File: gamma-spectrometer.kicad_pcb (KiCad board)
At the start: 2 copper layers, 140.3 x 36.5 mm, 71 parts, among them J1 *, J2 *, Q1 2N7002, Q3 MMBT5088LT1G, Q4 MMBT5088LT1G, U1 Pico 2, U10 MICROFC-60035-SMT-TR1, U2 OPA357AIDBVR, U3 TLV3201AIDBVR, U4 OPA357AIDBVR, U5 OPA357AIDBVR, U6 LM4040AIM3-3.0+T, U7 LM4040AIM3-3.0+T, U8 MAX5026EUT_T, U9 TPS7B6950DBVR

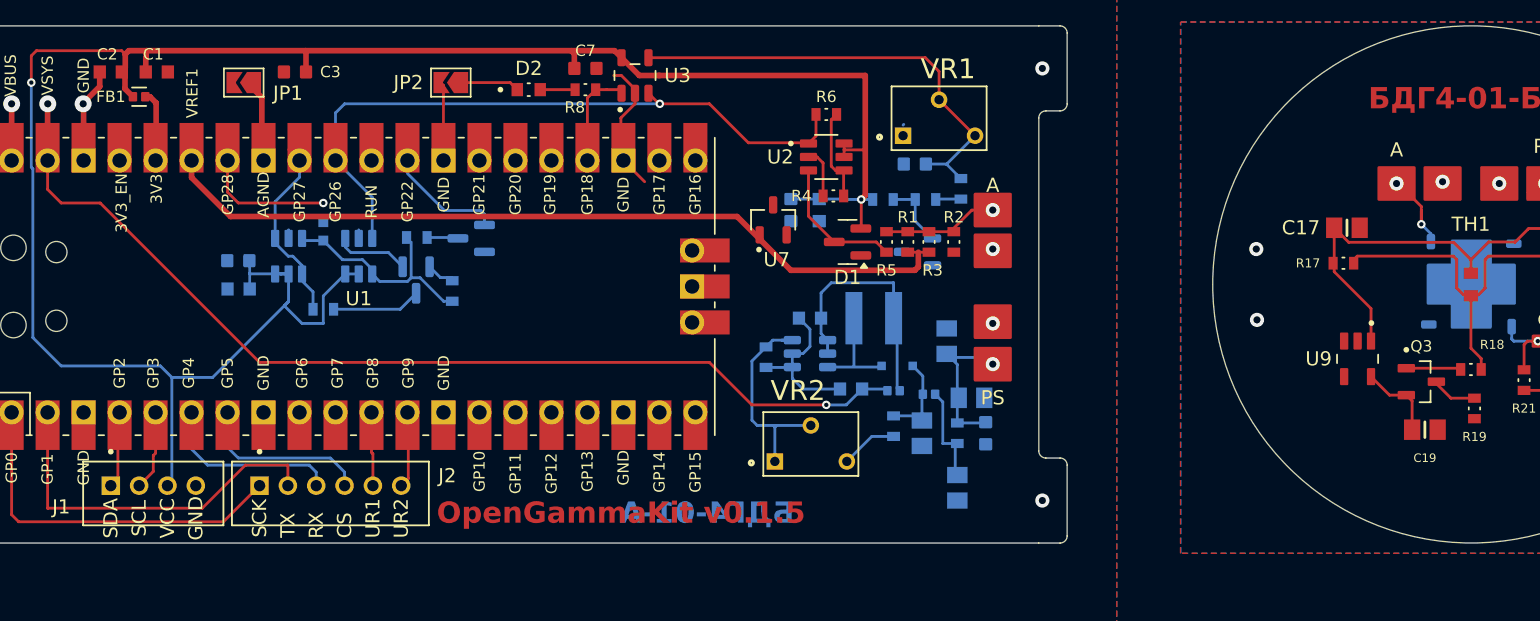
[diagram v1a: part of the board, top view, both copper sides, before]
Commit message: C17,C19,FB1,FB2,FB3 footprint fix
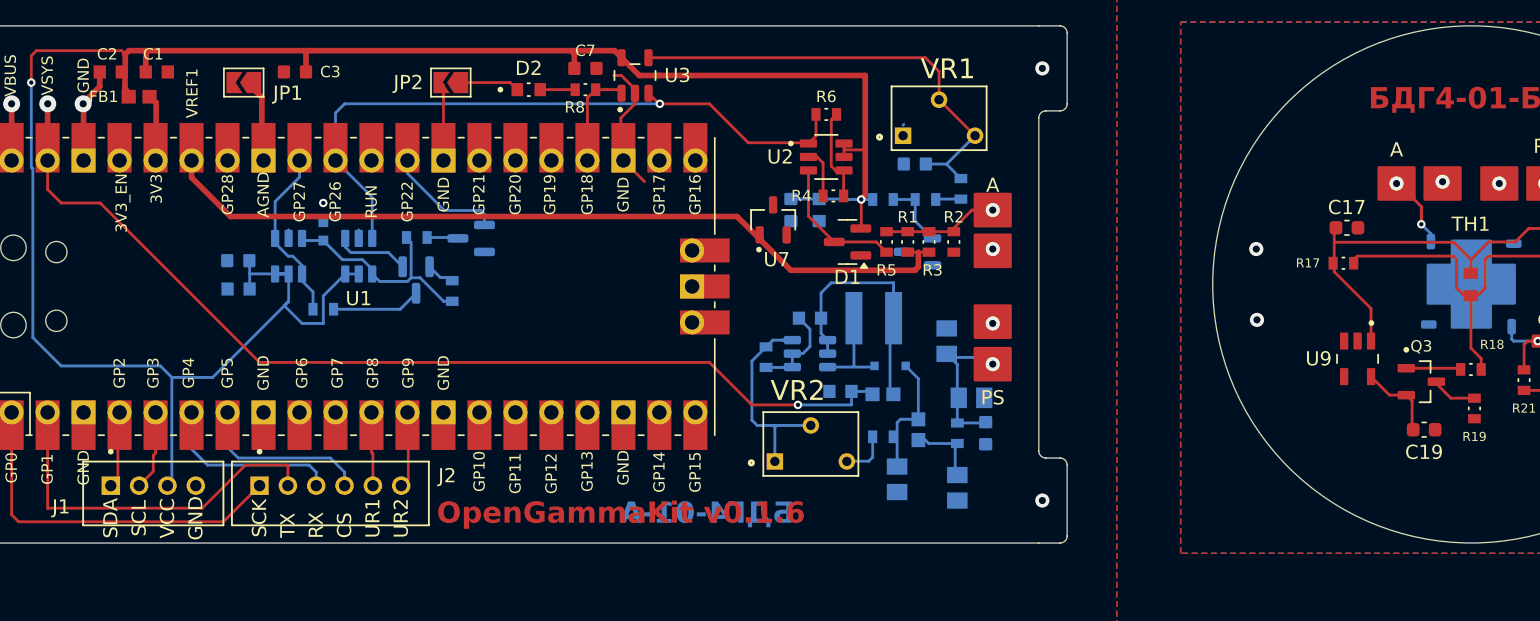
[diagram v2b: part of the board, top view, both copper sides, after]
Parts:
- C17, C19: footprint CL21A475KBQNNNE:CAPC2012X140N -> Capacitor_SMD:C_0603_1608Metric
- FB1, FB2, FB3: footprint ACML-0402HC-301-T:BEADC1005X65N -> BLM18KG102SN1D:BEADC1608X95N
- moved C12 3.69 mm to (152.0, 97.5)
- moved FB2 2.61 mm to (153.5, 94.0), turned to 90 degrees
- moved R15 1.06 mm to (151.0, 94.5), turned to 0 degrees
- moved FB3 0.79 mm to (151.0, 91.5)
- moved C18 0.77 mm to (148.0, 91.3)
- moved D5 0.50 mm to (151.5, 89.5)
- moved C19 0.05 mm to (189.2, 94.0)
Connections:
- net Net-(U8-VCC) renamed Vdrive
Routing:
- net GND: track 50.1 -> 36.4 mm
- net Net-(D5-K): track 6.31 -> 8.84 mm
- net Net-(C13-Pad1): track 7.06 -> 5.19 mm
- net Vdrive: track 18.0 -> 18.6 mm
- net Net-(VR2-CW): track 3.96 -> 3.35 mm
- net Net-(D5-A): track 8.37 -> 7.77 mm
- net +5V: track 72.2 -> 71.7 mm
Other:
- board text added: "OpenGammaKit v0.1.6"
- board text removed: "OpenGammaKit v0.1.5"

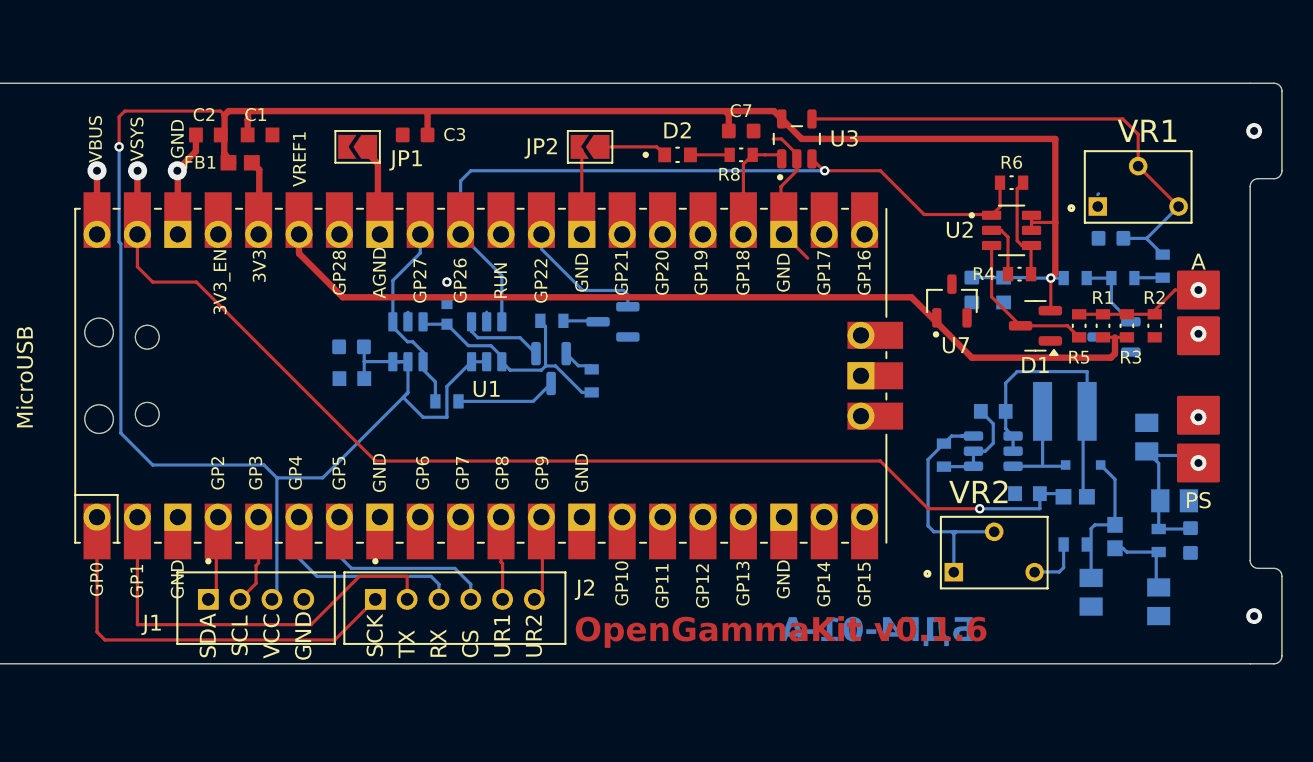
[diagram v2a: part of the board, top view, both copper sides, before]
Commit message: Switched to MAX1422 external ADC
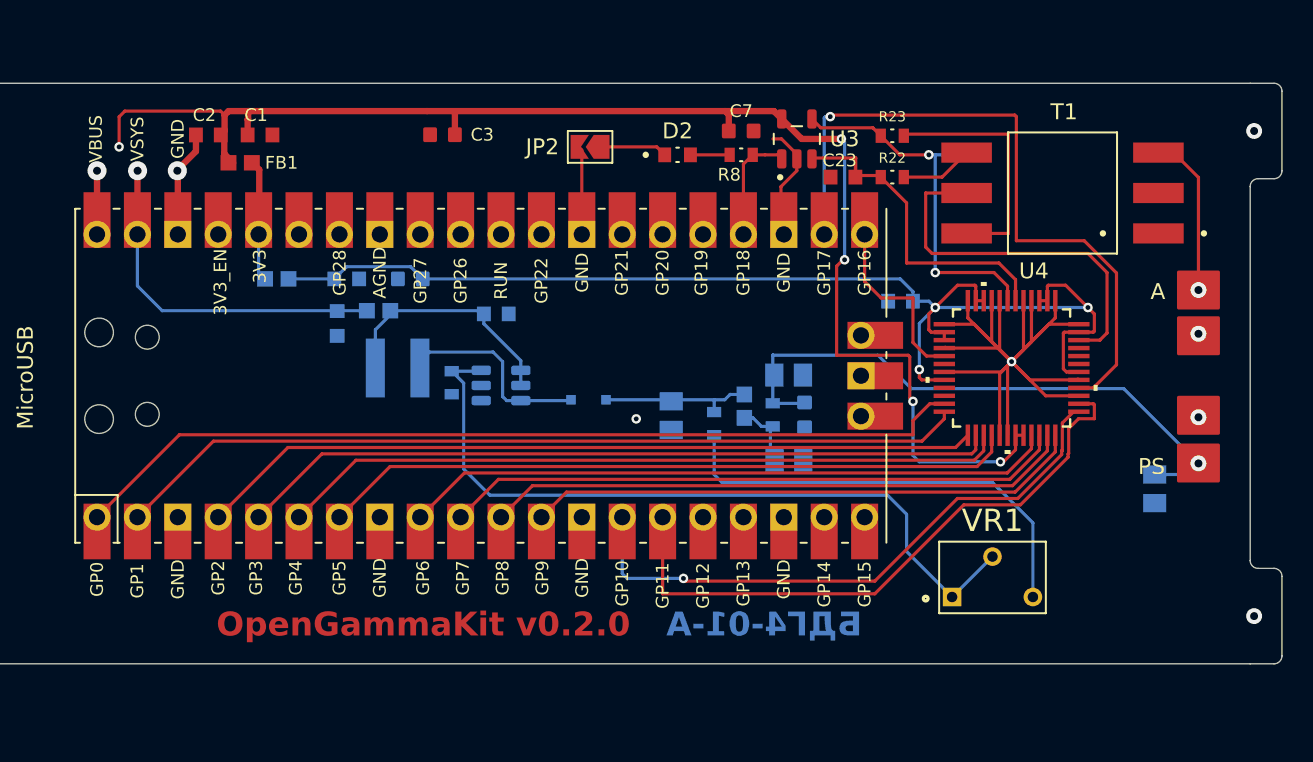
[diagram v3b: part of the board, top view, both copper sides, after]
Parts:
- removed C4: 22uF, CL10A226MP8NUNE:CAPC1608X90N
- removed C5, C6: 100n, CL10B104KC8NNNC:CAPC1608X90N
- removed D1, D3: BAT54S, Package_TO_SOT_SMD:SOT-23
- removed J1: *, B4B-PH-K-S_LF__SN_:JST_B4B-PH-K-S(LF)(SN)
- removed J2: *, B6B-PH-K-S_LF__SN_:JST_B6B-PH-K-S(LF)(SN)
- removed JP1: ~, Jumper:SolderJumper-2_P1.3mm_Open_TrianglePad1.0x1.5mm
- removed Q1: 2N7002, Package_TO_SOT_SMD:SOT-23
- removed R1, R3, R7, R9: 210k, ERJ3EKF2103V:RES_ERJ3EKF2103V
- removed R10, R5: 100R, ERJ3EKF1000V:RES_ERJ3EKF1000V
- removed R11: 10k, ERJ3EKF1002V:RES_ERJ3EKF1002V
- removed R12, R13, R2, R4, R6: 1k, ERJ3EKF1001V:RES_ERJ3EKF1001V
- removed U2, U5: OPA357AIDBVR, OPA357AIDBVR:SOT95P280X145-6N
- removed U6, U7: LM4040AIM3-3.0+T, LM4040AIM3-3_0-T:SOT95P237X112-3N
- removed VR2: 50k, 3266W-1-503:TRIM_3266W-1-503
- added C23: 22pF, ECJ-1VC1H220J:CAPC1608X90N, F.Cu at (136.4, 71.4)
- added C24: 22pF, ECJ-1VC1H220J:CAPC1608X90N, B.Cu at (144.2, 70.0)
- added FB4: BLM18KG102SN1D, BLM18KG102SN1D:BEADC1608X95N, B.Cu at (100.8, 77.8)
- added R22: 25.5R, ERJ3EKF25R5V:RES_ERJ3EKF25R5V, F.Cu at (139.5, 71.4)
- added R23: 25.5R, ERJ3EKF25R5V:RES_ERJ3EKF25R5V, F.Cu at (139.5, 68.8)
- added T1: T1-1T-KK81, T1-1T-KK81:XFMR_T1-1T-KK81_, F.Cu at (150.2, 72.4)
- C8: value 470p -> 22uF; footprint ECHU1C471JX5:CAP_ECHU1C471JX5 -> CL10A226MP8NUNE:CAPC1608X90N
- U4: value OPA357AIDBVR -> MAX1422ECM+D; footprint OPA357AIDBVR:SOT95P280X145-6N -> MAX1422ECM-D:21-0054G_48_MXM; moved to F.Cu
- moved FB3 45.3 mm to (107.2, 79.8)
- moved C18 44.7 mm to (104.6, 80.6), turned to -90 degrees
- moved L1 42.0 mm to (108.4, 83.4), turned to 180 degrees
- moved U4 33.0 mm to (147.0, 83.4)
- moved C11 31.8 mm to (114.6, 80.0), turned to 0 degrees
- moved D5 31.4 mm to (120.4, 85.4)
- moved R14 31.3 mm to (111.8, 84.3)
- moved U8 31.2 mm to (114.9, 84.5)
- moved C12 28.6 mm to (125.6, 86.4)
- moved C8 28.5 mm to (140.0, 79.2), turned to 180 degrees
- moved VR1 26.2 mm to (145.8, 97.8)
- moved C14 25.5 mm to (133.0, 83.8)
- moved C16 25.5 mm to (134.0, 86.3)
- moved R16 25.5 mm to (132.0, 86.3)
- moved C13 24.9 mm to (133.0, 89.2), turned to 0 degrees
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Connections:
- C10 pad 2: VCC -> AVDD
- C8 pad 1: GND -> AVDD
- C8 pad 2: Net-(U4--IN) -> GND
- C9 pad 1: VCC -> AVDD
- R15 pad 1: Net-(VR2-CW) -> Net-(VR1-CW)
- U1 pad 1: SCK -> /D0
- U1 pad 10: unconnected-(U1-GPIO7-Pad10)_1 -> /D7
- U1 pad 11: UART1TX -> /D8
- U1 pad 12: UART1RX -> /D9
- U1 pad 14: unconnected-(U1-GPIO10-Pad14) -> /D10
- U1 pad 15: unconnected-(U1-GPIO11-Pad15) -> /D11
- U1 pad 2: TX -> /D1
- U1 pad 21: unconnected-(U1-GPIO16-Pad21)_1 -> /CLK
- U1 pad 22: unconnected-(U1-GPIO17-Pad22)_1 -> /PD
- U1 pad 29: RST -> unconnected-(U1-GPIO22-Pad29)_1
- U1 pad 31: SIG -> unconnected-(U1-GPIO26_ADC0-Pad31)
- U1 pad 32: PEAK -> unconnected-(U1-GPIO27_ADC1-Pad32)_1
- U1 pad 33: Net-(JP1-A) -> GND
- U1 pad 34: GND -> unconnected-(U1-GPIO28_ADC2-Pad34)_1
- U1 pad 35: VREF1 -> unconnected-(U1-ADC_VREF-Pad35)_1
- U1 pad 4: SDA -> /D2
- U1 pad 5: SCL -> /D3
- U1 pad 6: RX -> /D4
- U1 pad 7: CS -> /D5
- U1 pad 9: unconnected-(U1-GPIO6-Pad9)_1 -> /D6
- U3 pad 3: SIG -> INP
- U3 pad 4: Net-(U3-IN-) -> INN
- U4 pad 1: Net-(D3-A) -> GND
- U4 pad 2: GND -> AVDD
- U4 pad 3: SIG -> AVDD
- U4 pad 4: Net-(U4--IN) -> GND
- U4 pad 5: VCC -> GND
- U4 pad 6: VCC -> INP
- VR1 pad 1: GND -> Net-(U8-FB)
- VR1 pad 2: Net-(U3-IN-) -> Net-(U8-FB)
- VR1 pad 3: Net-(U3-IN-) -> Net-(VR1-CW)
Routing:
- net AVDD: track 0.00 -> 77.6 mm, vias 0 -> 3
- net VCC: track 152.3 -> 89.1 mm, vias 2 -> 5
- net VREF1: track 57.8 -> 0.00 mm
- net /D0: track 0.00 -> 56.7 mm
- net /D1: track 0.00 -> 54.5 mm
- net GND: track 36.4 -> 90.4 mm, vias 6 -> 7
- net /D2: track 0.00 -> 49.4 mm
- net +5V: track 71.7 -> 22.5 mm, vias 2 -> 1
- net SIG: track 49.0 -> 0.00 mm, vias 1 -> 0
- net /D3: track 0.00 -> 47.8 mm
- net /D4: track 0.00 -> 45.8 mm
- net /D5: track 0.00 -> 44.4 mm
- net /PD: track 0.00 -> 43.0 mm, vias 0 -> 1
- net /D6: track 0.00 -> 41.1 mm
- net /D11: track 0.00 -> 39.4 mm
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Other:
- board text added: "OpenGammaKit v0.2.0"
- board text removed: "CS"
- board text removed: "GND"
- board text removed: "OpenGammaKit v0.1.6"
- board text removed: "RX"
- board text removed: "SCK"
- board text removed: "SCL"
- board text removed: "SDA"
- board text removed: "TX"
- board text removed: "UR1"
- board text removed: "UR2"
- board text removed: "VCC"
- board text removed: "VREF1"

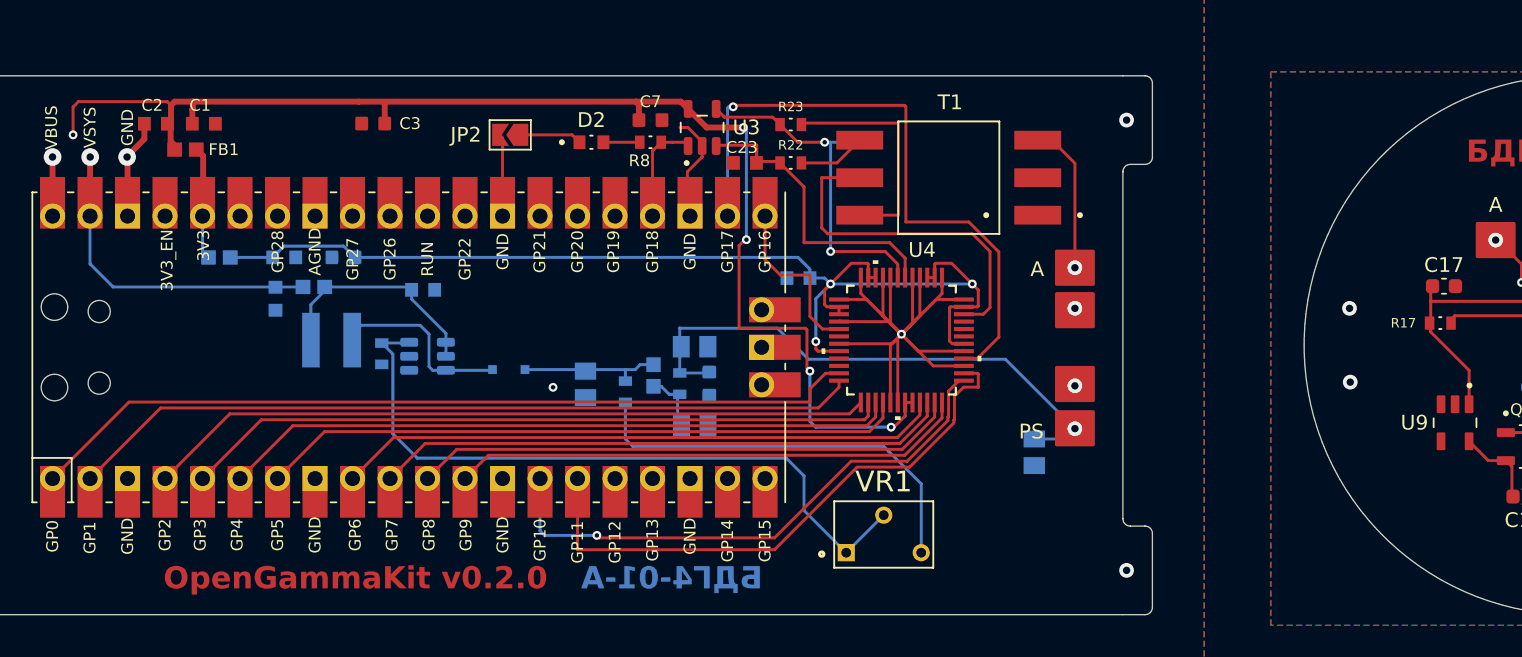
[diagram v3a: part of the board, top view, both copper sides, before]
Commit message: Updated 3d models
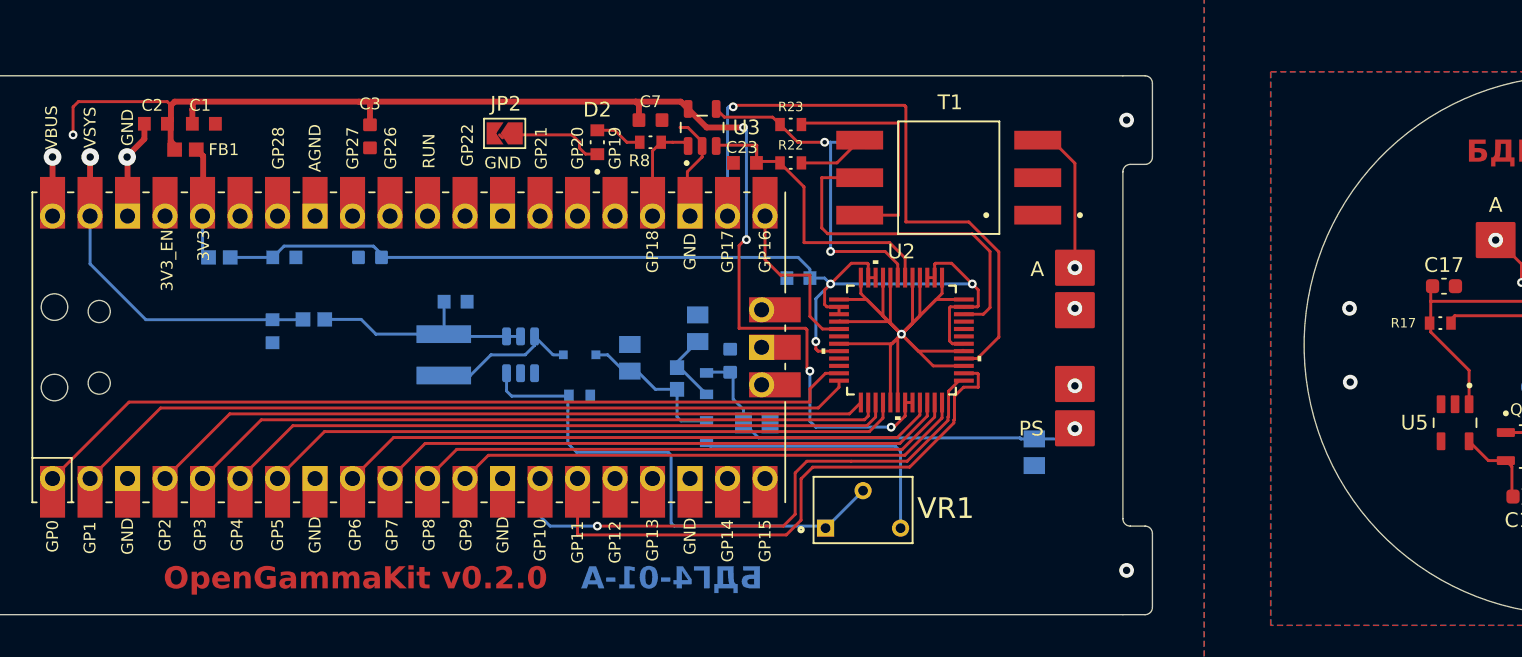
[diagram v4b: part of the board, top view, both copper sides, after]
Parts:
- moved R14 13.7 mm to (125.2, 87.2), turned to 180 degrees
- moved L1 7.67 mm to (116.0, 84.4), turned to 90 degrees
- moved C14 6.65 mm to (137.2, 89.0)
- moved C13 6.60 mm to (133.2, 82.6), turned to 90 degrees
- moved U4 6.30 mm to (121.2, 84.4), turned to 90 degrees
- moved R15 6.13 mm to (133.8, 89.6)
- moved D5 4.90 mm to (125.2, 84.4)
- moved C12 3.50 mm to (128.6, 84.6), turned to 90 degrees
- moved C11 2.34 mm to (116.8, 80.8)
- moved C18 2.21 mm to (104.4, 82.8)
- moved FB3 2.20 mm to (107.2, 82.0)
- moved VR1 2.17 mm to (144.4, 96.1)
- moved C16 2.10 mm to (135.4, 84.8), turned to -90 degrees
- moved R16 1.81 mm to (133.8, 86.3)
- moved C10 1.80 mm to (111.0, 77.8)
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- renumbered U4 to U2, U8 to U4, U9 to U5, U10 to U6
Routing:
- net Net-(U4-FB): track 47.3 -> 34.8 mm
- net Net-(VR1-CW): track 28.6 -> 18.6 mm
- net PS_OUT: track 38.0 -> 29.3 mm
- net GND: track 90.4 -> 85.7 mm, vias 7 -> 6
- net Net-(D5-A): track 12.4 -> 10.1 mm
- net Net-(JP2-A): track 4.17 -> 6.24 mm
- net +5V: track 22.5 -> 23.4 mm
- net Vdrive: track 15.1 -> 16.0 mm
- net Net-(D5-K): track 9.61 -> 10.4 mm
- net Net-(C13-Pad1): track 4.51 -> 5.33 mm
- net Net-(D2-PadA): track 2.47 -> 3.21 mm
